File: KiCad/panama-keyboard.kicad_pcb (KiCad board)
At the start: 2 copper layers, 304.8 x 124.6 mm, 172 parts, among them J1 MX, J2 USB_C_Receptacle_USB2.0, J3 AVR-ISP-6, K1 MX, M1 MX, P1 MX, Q1 MX, T1 MX, U1 MX, U2 ATmega32A-PU, X1 MX, Y1 MX, Y2 Crystal

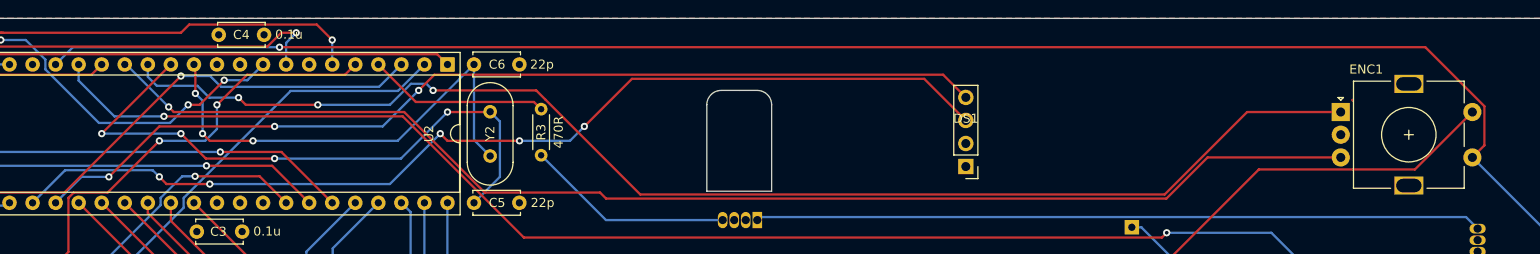
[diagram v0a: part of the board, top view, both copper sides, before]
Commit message: pinout changed, pcb trace to be reworked
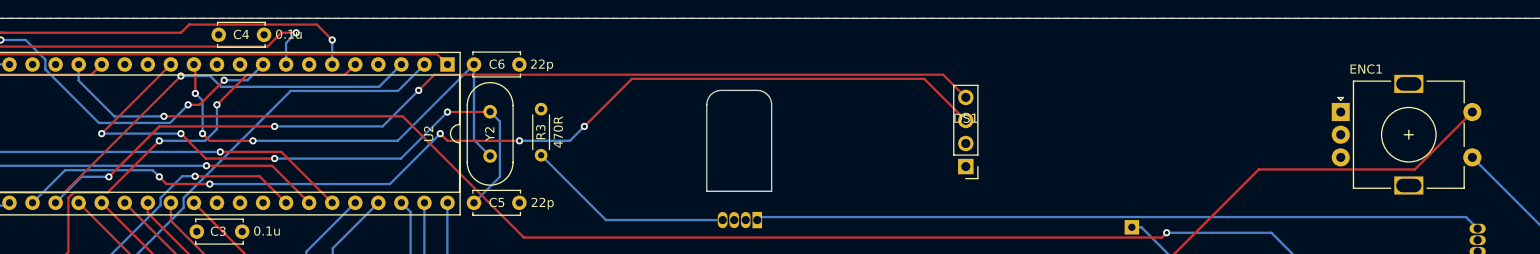
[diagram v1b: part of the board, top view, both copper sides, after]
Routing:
- net col14: track 205.9 -> 38.8 mm, vias 1 -> 0
- net enc-A: track 143.9 -> 0.00 mm, vias 3 -> 0
- net enc-B: track 142.1 -> 0.00 mm, vias 1 -> 0
- net LED: track 20.0 -> 0.00 mm

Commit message: traces removed for new pinout
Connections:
- D77 pad 1: (no net) -> Net-(D77-Pad1)
- J2 pad A8: (no net) -> Net-(J2-PadA8)
- J2 pad B8: (no net) -> Net-(J2-PadB8)
- U2 pad 1: col3 -> enc-A
- U2 pad 14: enc-A -> row2
- U2 pad 15: enc-B -> row1
- U2 pad 17: col13 -> D-
- U2 pad 18: col14 -> Net-(U2-Pad18)
- U2 pad 19: (no net) -> boot
- U2 pad 2: col4 -> enc-B
- U2 pad 20: boot -> row0
- U2 pad 21: D- -> col0
- U2 pad 24: col7 -> col1
- U2 pad 25: col8 -> col2
- U2 pad 26: col9 -> col3
- U2 pad 27: col10 -> col4
- U2 pad 28: col11 -> col5
- U2 pad 29: col12 -> col6
- U2 pad 3: col5 -> LED
- U2 pad 32: (no net) -> Net-(U2-Pad32)
- U2 pad 33: col2 -> col7
- U2 pad 34: col1 -> col8
- U2 pad 35: col0 -> col9
- U2 pad 36: row4 -> col10
- U2 pad 37: row3 -> col11
- U2 pad 38: row2 -> col12
- U2 pad 39: row1 -> col13
- U2 pad 4: LED -> row4
- U2 pad 40: row0 -> col14
- U2 pad 5: col6 -> row3
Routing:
- net col0: track 249.2 -> 0.00 mm, vias 2 -> 0
- net col13: track 243.2 -> 0.00 mm, vias 2 -> 0
- net col3: track 229.9 -> 0.00 mm
- net col1: track 227.3 -> 0.00 mm, vias 2 -> 0
- net col2: track 202.1 -> 0.00 mm, vias 1 -> 0
- net col12: track 192.3 -> 0.00 mm
- net col4: track 159.3 -> 0.00 mm
- net reset: track 138.2 -> 0.00 mm, vias 3 -> 0
- net col5: track 138.1 -> 0.00 mm, vias 1 -> 0
- net MOSI: track 134.3 -> 0.00 mm, vias 3 -> 0
- net SCK: track 134.3 -> 0.00 mm, vias 2 -> 0
- net col6: track 118.0 -> 0.00 mm, vias 2 -> 0
- net SCL: track 112.3 -> 0.00 mm, vias 5 -> 0
- net SDA: track 107.2 -> 0.00 mm, vias 3 -> 0
- net row4: track 387.3 -> 285.0 mm, vias 2 -> 0
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
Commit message: pcb rework done
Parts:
- removed G*** (x2): LOGO, LOGO:merciertech600
- moved Y2 4.79 mm to (328.6, 148.4), turned to 90 degrees
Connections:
- D77 pad 1: Net-(D77-Pad1) -> (no net)
- J2 pad A8: Net-(J2-PadA8) -> (no net)
- J2 pad B8: Net-(J2-PadB8) -> (no net)
- U2 pad 18: Net-(U2-Pad18) -> (no net)
- U2 pad 32: Net-(U2-Pad32) -> (no net)
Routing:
- net col0: track 0.00 -> 202.9 mm
- net col1: track 0.00 -> 200.0 mm
- net col3: track 0.00 -> 195.8 mm
- net col13: track 0.00 -> 194.4 mm, vias 0 -> 1
- net col2: track 0.00 -> 181.9 mm
- net col12: track 0.00 -> 169.4 mm
- net MISO: track 0.00 -> 144.3 mm, vias 0 -> 2
- net MOSI: track 0.00 -> 140.9 mm, vias 0 -> 2
- net SCK: track 0.00 -> 134.9 mm
- net reset: track 0.00 -> 134.5 mm, vias 0 -> 2
- net col4: track 0.00 -> 124.1 mm
- net col14: track 38.8 -> 156.7 mm, vias 0 -> 2
- net row4: track 285.0 -> 402.9 mm, vias 0 -> 2
- net SCL: track 0.00 -> 110.0 mm, vias 0 -> 2
- net SDA: track 0.00 -> 107.1 mm, vias 0 -> 3
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
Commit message: pcb height adjust
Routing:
- removed copper zone on F.Cu, net +5V
- removed copper zone on B.Cu, net GND
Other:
- board size 304.8 x 124.6 mm -> 304.8 x 123.8 mm
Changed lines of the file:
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@@
   (general
     (thickness 1.6)
-    (drawings 63)
+    (drawings 68)
     (tracks 903)
     (zones 0)
@@
     (47 F.CrtYd user)
     (48 B.Fab user hide)
-    (49 F.Fab user hide)
+    (49 F.Fab user)
   )
   (setup
@@
     )
   )
+  (dimension 304.8 (width 0.15) (layer Dwgs.User)
+    (gr_text "304.800 mm" (at 304.00625 268.793749) (layer Dwgs.User)
+      (effects (font (size 1 1) (thickness 0.15)))
+    )
+    (feature1 (pts (xy 456.40625 254) (xy 456.40625 268.08017)))
+    (feature2 (pts (xy 151.60625 254) (xy 151.60625 268.08017)))
+    (crossbar (pts (xy 151.60625 267.493749) (xy 456.40625 267.493749)))
+    (arrow1a (pts (xy 456.40625 267.493749) (xy 455.279746 268.08017)))
+    (arrow1b (pts (xy 456.40625 267.493749) (xy 455.279746 266.907328)))
+    (arrow2a (pts (xy 151.60625 267.493749) (xy 152.732754 268.08017)))
+    (arrow2b (pts (xy 151.60625 267.493749) (xy 152.732754 266.907328)))
+  )
+  (dimension 123.825 (width 0.15) (layer Dwgs.User)
+    (gr_text "123.825 mm" (at 464.05625 195.2625 270) (layer Dwgs.User)
+      (effects (font (size 1 1) (thickness 0.15)))
+    )
+    (feature1 (pts (xy 453.23125 257.175) (xy 463.342671 257.175)))
+    (feature2 (pts (xy 453.23125 133.35) (xy 463.342671 133.35)))
+    (crossbar (pts (xy 462.75625 133.35) (xy 462.75625 257.175)))
+    (arrow1a (pts (xy 462.75625 257.175) (xy 462.169829 256.048496)))
+    (arrow1b (pts (xy 462.75625 257.175) (xy 463.342671 256.048496)))
+    (arrow2a (pts (xy 462.75625 133.35) (xy 462.169829 134.476504)))
+    (arrow2b (pts (xy 462.75625 133.35) (xy 463.342671 134.476504)))
+  )
+  (gr_arc (start 453.23125 136.525) (end 456.40625 136.525) (angle -90) (layer Edge.Cuts) (width 0.05))
+  (dimension 123.825 (width 0.15) (layer Dwgs.User)
+    (gr_text "123.825 mm" (at 139.19375 195.2625 90) (layer Dwgs.User)
+      (effects (font (size 1 1) (thickness 0.15)))
+    )
+    (feature1 (pts (xy 154.78125 133.35) (xy 139.907329 133.35)))
+    (feature2 (pts (xy 154.78125 257.175) (xy 139.907329 257.175)))
+    (crossbar (pts (xy 140.49375 257.175) (xy 140.49375 133.35)))
+    (arrow1a (pts (xy 140.49375 133.35) (xy 141.080171 134.476504)))
+    (arrow1b (pts (xy 140.49375 133.35) (xy 139.907329 134.476504)))
+    (arrow2a (pts (xy 140.49375 257.175) (xy 141.080171 256.048496)))
+    (arrow2b (pts (xy 140.49375 257.175) (xy 139.907329 256.048496)))
+  )
+  (gr_arc (start 453.23125 254) (end 453.23125 257.175) (angle -90) (layer Edge.Cuts) (width 0.05))
+  (gr_arc (start 154.78125 254) (end 151.60625 254) (angle -90) (layer Edge.Cuts) (width 0.05))
+  (dimension 4.572 (width 0.15) (layer Dwgs.User)
+    (gr_text "4.572 mm" (at 242.346 254.889 270) (layer Dwgs.User)
+      (effects (font (size 1 1) (thickness 0.15)))
+    )
+    (feature1 (pts (xy 232.537 257.175) (xy 241.632421 257.175)))
+    (feature2 (pts (xy 232.537 252.603) (xy 241.632421 252.603)))
+    (crossbar (pts (xy 241.046 252.603) (xy 241.046 257.175)))
+    (arrow1a (pts (xy 241.046 257.175) (xy 240.459579 256.048496)))
+    (arrow1b (pts (xy 241.046 257.175) (xy 241.632421 256.048496)))
+    (arrow2a (pts (xy 241.046 252.603) (xy 240.459579 253.729504)))
+    (arrow2b (pts (xy 241.046 252.603) (xy 241.632421 253.729504)))
+  )
+  (dimension 38.242 (width 0.15) (layer Dwgs.User)
+    (gr_text "38.242 mm" (at 398.283 128.875001) (layer Dwgs.User)
+      (effects (font (size 1 1) (thickness 0.15)))
+    )
+    (feature1 (pts (xy 379.162 140.27725) (xy 379.162 129.58858)))
+    (feature2 (pts (xy 417.404 140.27725) (xy 417.404 129.58858)))
+    (crossbar (pts (xy 417.404 130.175001) (xy 379.162 130.175001)))
+    (arrow1a (pts (xy 379.162 130.175001) (xy 380.288504 129.58858)))
+    (arrow1b (pts (xy 379.162 130.175001) (xy 380.288504 130.761422)))
+    (arrow2a (pts (xy 417.404 130.175001) (xy 416.277496 129.58858)))
+    (arrow2b (pts (xy 417.404 130.175001) (xy 416.277496 130.761422)))
+  )
+  (dimension 304.801034 (width 0.15) (layer Dwgs.User)
+    (gr_text "304.801 mm" (at 303.97707 124.922859 0.1492074219) (layer Dwgs.User)
+      (effects (font (size 1 1) (thickness 0.15)))
+    )
+    (feature1 (pts (xy 151.60625 136.525) (xy 151.578928 126.033311)))
+    (feature2 (pts (xy 456.40625 135.73125) (xy 456.378928 125.239561)))
+    (crossbar (pts (xy 456.380455 125.82598) (xy 151.580455 126.61973)))
+    (arrow1a (pts (xy 151.580455 126.61973) (xy 152.705428 126.030378)))
+    (arrow1b (pts (xy 151.580455 126.61973) (xy 152.708482 127.203215)))
+    (arrow2a (pts (xy 456.380455 125.82598) (xy 455.252428 125.242495)))
+    (arrow2b (pts (xy 456.380455 125.82598) (xy 455.255482 126.415332)))
+  )
   (gr_text USB-C (at 170.688 136.398) (layer F.SilkS)
     (effects (font (size 1 1) (thickness 0.15)))
@@
     (effects (font (size 1 1) (thickness 0.15)))
   )
-  (gr_arc (start 153.9875 255.5875) (end 151.60625 255.5875) (angle -90) (layer Edge.Cuts) (width 0.05))
-  (gr_arc (start 454.025 255.5875) (end 454.025 257.96875) (angle -90) (layer Edge.Cuts) (width 0.05))
-  (gr_arc (start 454.025 135.73125) (end 456.40625 135.73125) (angle -90) (layer Edge.Cuts) (width 0.05))
   (gr_arc (start 154.78125 136.525) (end 154.78125 133.35) (angle -90) (layer Edge.Cuts) (width 0.05))
   (gr_line (start 246.85625 145.25625) (end 246.85625 150.8125) (layer Dwgs.User) (width 0.15))
@@
   (gr_line (start 350.8375 146.05) (end 350.8375 149.225) (layer Dwgs.User) (width 0.15))
   (gr_line (start 361.15625 145.25625) (end 361.15625 149.225) (layer Dwgs.User) (width 0.15))
-  (dimension 3.048 (width 0.15) (layer Dwgs.User)
-    (gr_text "3.048 mm" (at 227.681001 256.286 270) (layer Dwgs.User)
-      (effects (font (size 1 1) (thickness 0.15)))
-    )
-    (feature1 (pts (xy 232.537 257.81) (xy 228.39458 257.81)))
-    (feature2 (pts (xy 232.537 254.762) (xy 228.39458 254.762)))
-    (crossbar (pts (xy 228.981001 254.762) (xy 228.981001 257.81)))
-    (arrow1a (pts (xy 228.981001 257.81) (xy 228.39458 256.683496)))
-    (arrow1b (pts (xy 228.981001 257.81) (xy 229.567422 256.683496)))
-    (arrow2a (pts (xy 228.981001 254.762) (xy 228.39458 255.888504)))
-    (arrow2b (pts (xy 228.981001 254.762) (xy 229.567422 255.888504)))
-  )
   (gr_arc (start 357.98125 142.875) (end 359.56875 142.875) (angle -90) (layer Edge.Cuts) (width 0.05))
   (gr_arc (start 354.0125 142.875) (end 354.0125 141.2875) (angle -90) (layer Edge.Cuts) (width 0.05))
@@
     (arrow2b (pts (xy 252.015836 115.887501) (xy 250.889332 116.473922)))
   )
-  (gr_line (start 454.025 133.35) (end 154.78125 133.35) (layer Edge.Cuts) (width 0.05))
+  (gr_line (start 453.23125 133.35) (end 154.78125 133.35) (layer Edge.Cuts) (width 0.05))
   (gr_line (start 361.15625 109.5375) (end 361.15625 127.79375) (layer F.Fab) (width 0.05))
   (gr_line (start 350.8375 110.33125) (end 350.8375 127.79375) (layer F.Fab) (width 0.05))
@@
   (gr_line (start 463.55 124.206) (end 463.55 124.206) (layer Edge.Cuts) (width 0.05))
   (gr_line (start 299.24375 278.60625) (end 299.24375 23.01875) (layer F.Fab) (width 0.15))
-  (gr_line (start 151.60625 255.5875) (end 151.60625 136.525) (layer Edge.Cuts) (width 0.05))
-  (gr_line (start 456.40625 255.5875) (end 456.40625 135.73125) (layer Edge.Cuts) (width 0.05))
-  (gr_line (start 153.9875 257.96875) (end 454.025 257.96875) (layer Edge.Cuts) (width 0.05))
+  (gr_line (start 151.60625 254) (end 151.60625 136.525) (layer Edge.Cuts) (width 0.05))
+  (gr_line (start 456.40625 254) (end 456.40625 136.525) (layer Edge.Cuts) (width 0.05))
+  (gr_line (start 154.78125 257.175) (end 453.23125 257.175) (layer Edge.Cuts) (width 0.05))
   (segment (start 333.53375 225.058962) (end 339.138538 230.66375) (width 0.254) (layer F.Cu) (net 1))
   (segment (start 339.138538 230.66375) (end 346.86875 230.66375) (width 0.254) (layer F.Cu) (net 1))
@@
   (segment (start 178.313738 150.01875) (end 172.13125 143.836262) (width 0.254) (layer F.Cu) (net 120))
   (segment (start 200.50125 150.01875) (end 178.313738 150.01875) (width 0.254) (layer F.Cu) (net 120))
-  (zone (net 30) (net_name GND) (layer B.Cu) (hatch edge 0.508)
-    (connect_pads (clearance 0.508))
-    (min_thickness 0.254)
-    (fill yes (arc_segments 32) (thermal_gap 0.508) (thermal_bridge_width 0.508))
-    (polygon
-      (pts
-        (xy 456.40625 257.96875) (xy 151.60625 257.96875) (xy 151.60625 133.35) (xy 456.40625 133.35)
-      )
-    )
-  )
-  (zone (net 31) (net_name +5V) (layer F.Cu) (hatch edge 0.508)
-    (connect_pads (clearance 0.508))
-    (min_thickness 0.254)
-    (fill yes (arc_segments 32) (thermal_gap 0.508) (thermal_bridge_width 0.508))
-    (polygon
-      (pts
-        (xy 456.40625 257.96875) (xy 151.60625 257.96875) (xy 151.60625 133.35) (xy 456.40625 133.35)
-      )
-    )
-  )
 )

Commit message: silkscreen pcb update
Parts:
- added G***: LOGO, LOGO:merciertech600-SymbOnly, F.Cu at (227.0, 140.5)
- added G***: LOGO, LOGO:merciertech600, B.Cu at (253.2, 245.3)
- Y2: value Crystal -> 16MHz
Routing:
- added copper zone on F.Cu, net +5V
- added copper zone on B.Cu, net GND
